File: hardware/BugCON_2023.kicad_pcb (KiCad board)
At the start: 2 copper layers, 99.7 x 79.7 mm, 1 part

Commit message: Add_Schematic
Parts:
- removed the Ref** at (126.6, 83.7)
- added Ref**: Val**, FootprintsB:Bugcon10, F.Cu at (143.1, 78.9)
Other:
- board outline removed

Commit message: Add_PCB
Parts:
- added C1: 1uF, Capacitor_SMD:C_0603_1608Metric, B.Cu at (154.4, 74.2)
- added C2: 10uF, Capacitor_SMD:C_0603_1608Metric, B.Cu at (157.5, 74.2)
- added C3: 10uF, Capacitor_SMD:C_0603_1608Metric, B.Cu at (156.0, 74.2)
- added C4: 10uF, Capacitor_SMD:C_0603_1608Metric, B.Cu at (141.5, 48.5)
- added C5: 10uF, Capacitor_SMD:C_0603_1608Metric, B.Cu at (141.5, 43.4)
- added C6: 0.1uF, Capacitor_SMD:C_0603_1608Metric, F.Cu at (136.1, 93.5)
- added C7: 0.1uF, Capacitor_SMD:C_0603_1608Metric, F.Cu at (149.9, 93.5)
- added C8: 0.1uF, Capacitor_SMD:C_0603_1608Metric, F.Cu at (123.5, 83.8)
- added C9: 0.1uF, Capacitor_SMD:C_0603_1608Metric, F.Cu at (163.1, 83.6)
- added D1: MBR120, Diode_SMD:D_SOD-123F, B.Cu at (137.4, 46.5)
- added D2: WS2812B, FootprintsB:WS2812B_WDS, F.Cu at (124.7, 87.4)
- added D6: WS2812B, FootprintsB:WS2812B_WDS, F.Cu at (137.4, 97.2)
- added D7: WS2812B, FootprintsB:WS2812B_WDS, F.Cu at (151.0, 97.2)
- added D8: WS2812B, FootprintsB:WS2812B_WDS, F.Cu at (164.2, 87.3)
- added F1: 0.5A, Fuse:Fuse_0805_2012Metric, B.Cu at (148.1, 109.5)
- added J1: Conn_01x04_Pin, Connector_PinSocket_2.54mm:PinSocket_1x04_P2.54mm_Vertical, F.Cu at (104.4, 75.7)
- added J2: Conn_01x04_Pin, Connector_PinSocket_2.54mm:PinSocket_1x04_P2.54mm_Vertical, F.Cu at (182.9, 77.0)
- added J3: Conn_01x02, Connector_PinSocket_2.54mm:PinSocket_1x02_P2.54mm_Vertical, B.Cu at (130.0, 46.2)
- added P1: USB_C_Plug_USB2.0, Connector_USB:USB_C_Receptacle_G-Switch_GT-USB-7010ASV, B.Cu at (144.3, 117.8)
- added Q1: DMG3415U-7, Package_TO_SOT_SMD:SOT-23, B.Cu at (134.1, 46.2)
- added R1: 10K, Resistor_SMD:R_0603_1608Metric, B.Cu at (191.5, 71.4)
- added R2: 5k1, Resistor_SMD:R_0603_1608Metric, B.Cu at (148.1, 111.3)
- added R3: 5k1, Resistor_SMD:R_0603_1608Metric, B.Cu at (140.5, 111.3)
- added R4: 100K, Resistor_SMD:R_0603_1608Metric, B.Cu at (136.7, 43.2)
- added R9: 470, Resistor_SMD:R_0603_1608Metric, F.Cu at (144.8, 94.7)
- added SW1: RESET, Button_Switch_SMD:SW_SPST_TL3342, B.Cu at (197.4, 69.3)
- added SW2: GPIO, Button_Switch_SMD:SW_SPST_TL3342, B.Cu at (91.2, 69.8)
- added SW3: ON, FootprintsB:SW-TH_SK12D07VG4, B.Cu at (144.0, 39.6)
- added U1: ESP32-S3-WROOM-1U-N16, FootprintsB:XCVR_ESP32-S3-WROOM-1-N8R2, B.Cu at (143.1, 78.7)
- added U2: AP2112K-3.3, Package_TO_SOT_SMD:SOT-23-5, B.Cu at (140.8, 46.0)

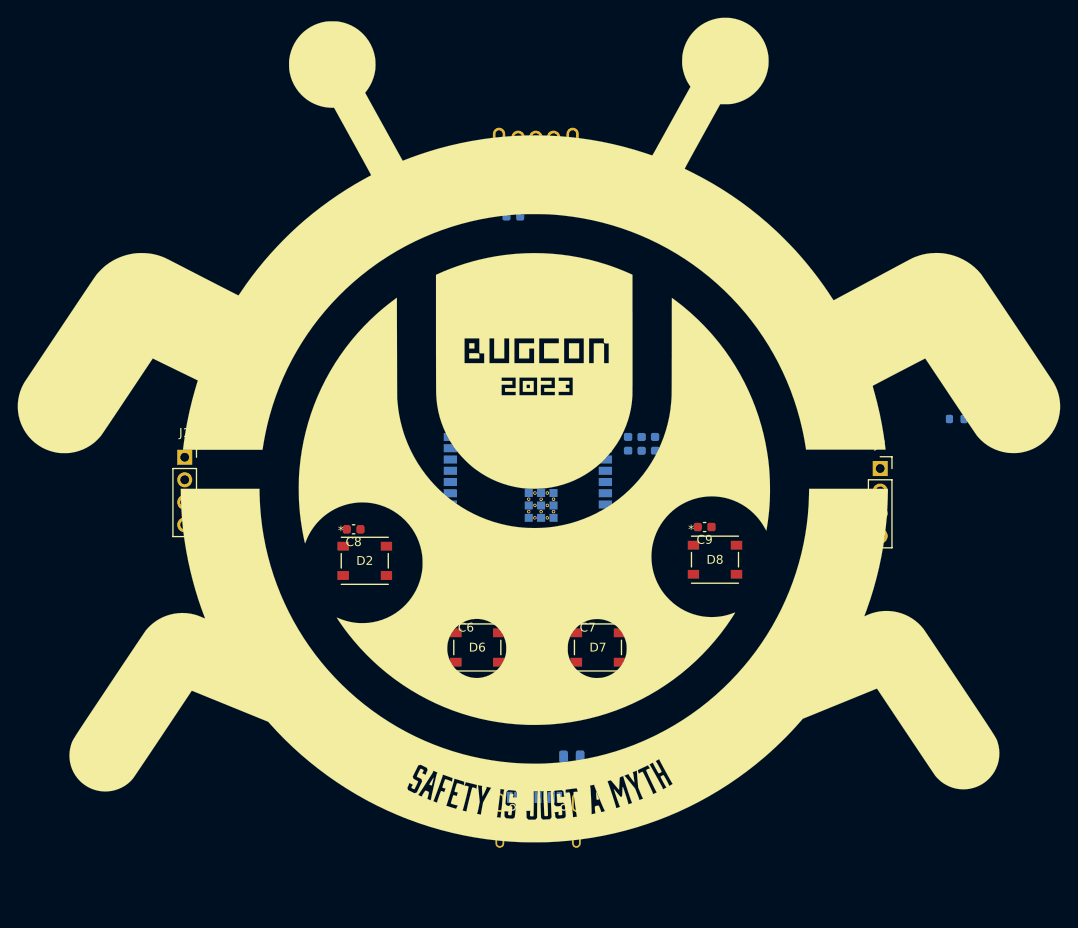
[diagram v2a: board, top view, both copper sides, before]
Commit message: Add_battery_holder
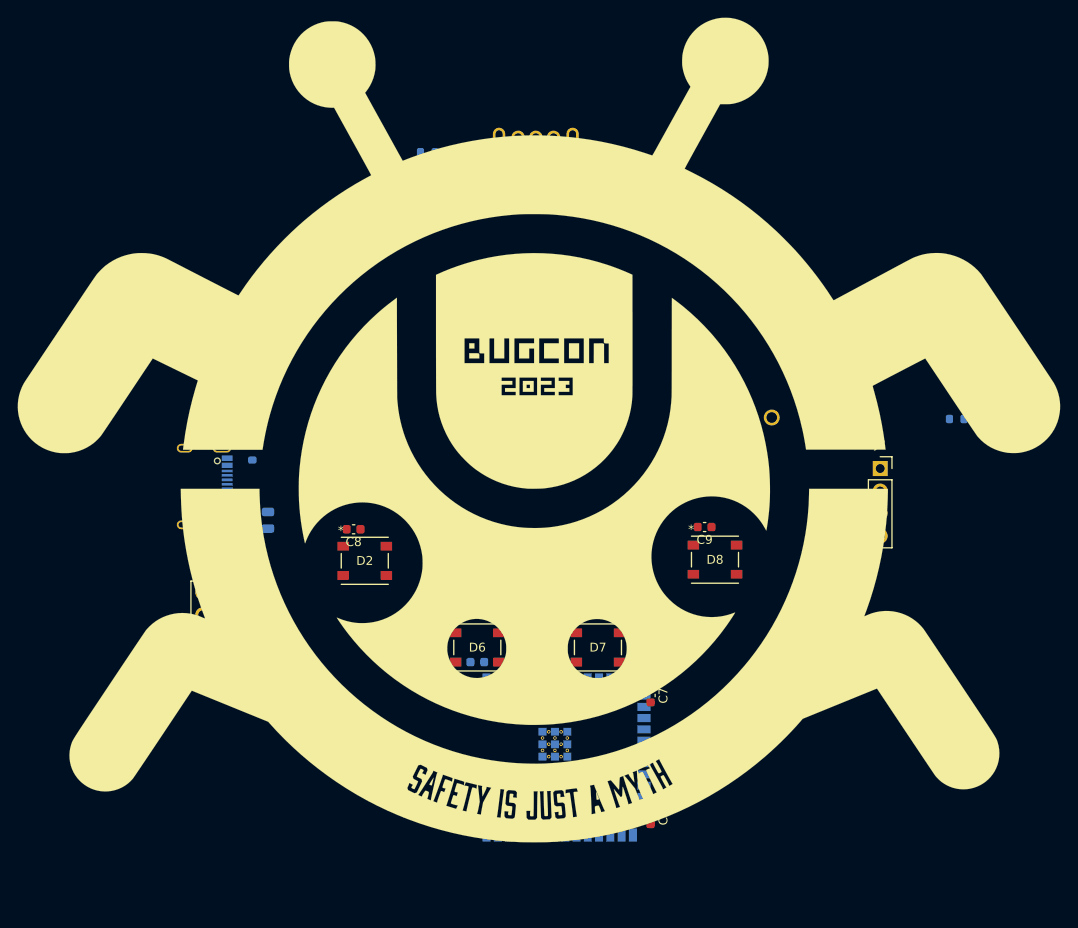
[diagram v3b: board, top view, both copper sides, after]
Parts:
- removed J3: Conn_01x02, Connector_PinSocket_2.54mm:PinSocket_1x02_P2.54mm_Vertical
- added J4: Battery, FootprintsB:BAT_12BH331P-GR, B.Cu at (143.9, 73.4)
- moved P1 54.9 mm to (105.5, 79.0), turned to 90 degrees
- moved R3 45.9 mm to (112.0, 75.2), turned to -90 degrees
- moved R2 45.9 mm to (112.0, 82.8), turned to 90 degrees
- moved F1 43.4 mm to (113.8, 82.8), turned to -90 degrees
- moved C2 31.8 mm to (137.4, 98.8), turned to 180 degrees
- moved C6 30.9 mm to (157.0, 116.3), turned to -90 degrees
- moved U1 30.9 mm to (143.7, 109.6), turned to -90 degrees
- moved C3 29.1 mm to (140.5, 98.8), turned to 0 degrees
- moved C1 27.0 mm to (143.5, 98.8), turned to 0 degrees
- moved J1 12.9 mm to (106.4, 88.4)
- moved C7 11.5 mm to (157.0, 102.6), turned to -90 degrees
- moved C4 5.19 mm to (136.7, 46.6)
- moved C5 5.19 mm to (136.7, 41.5)
- moved D1 5.19 mm to (132.6, 44.6)
- moved Q1 5.19 mm to (129.3, 44.3)
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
